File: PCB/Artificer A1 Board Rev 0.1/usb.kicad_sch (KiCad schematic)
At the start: 8 parts, among them U11 CH217K, U3 CH334F_C5187527, X1 SMD-3225_4P12M12PF10PPM

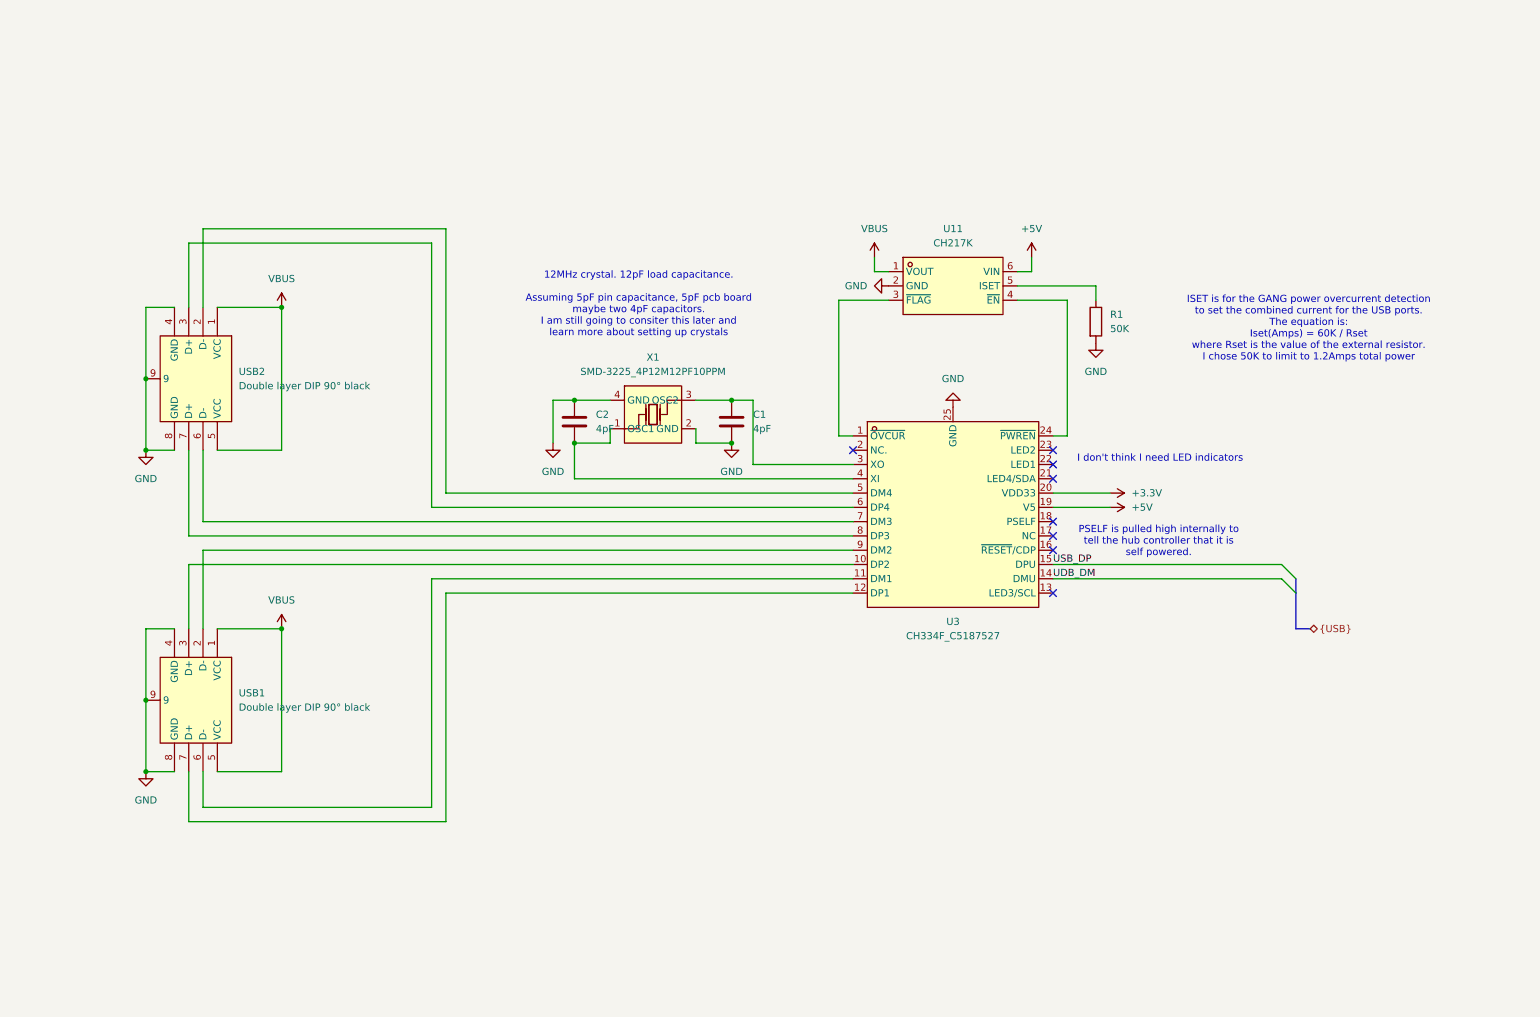
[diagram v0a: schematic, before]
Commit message: schematic update
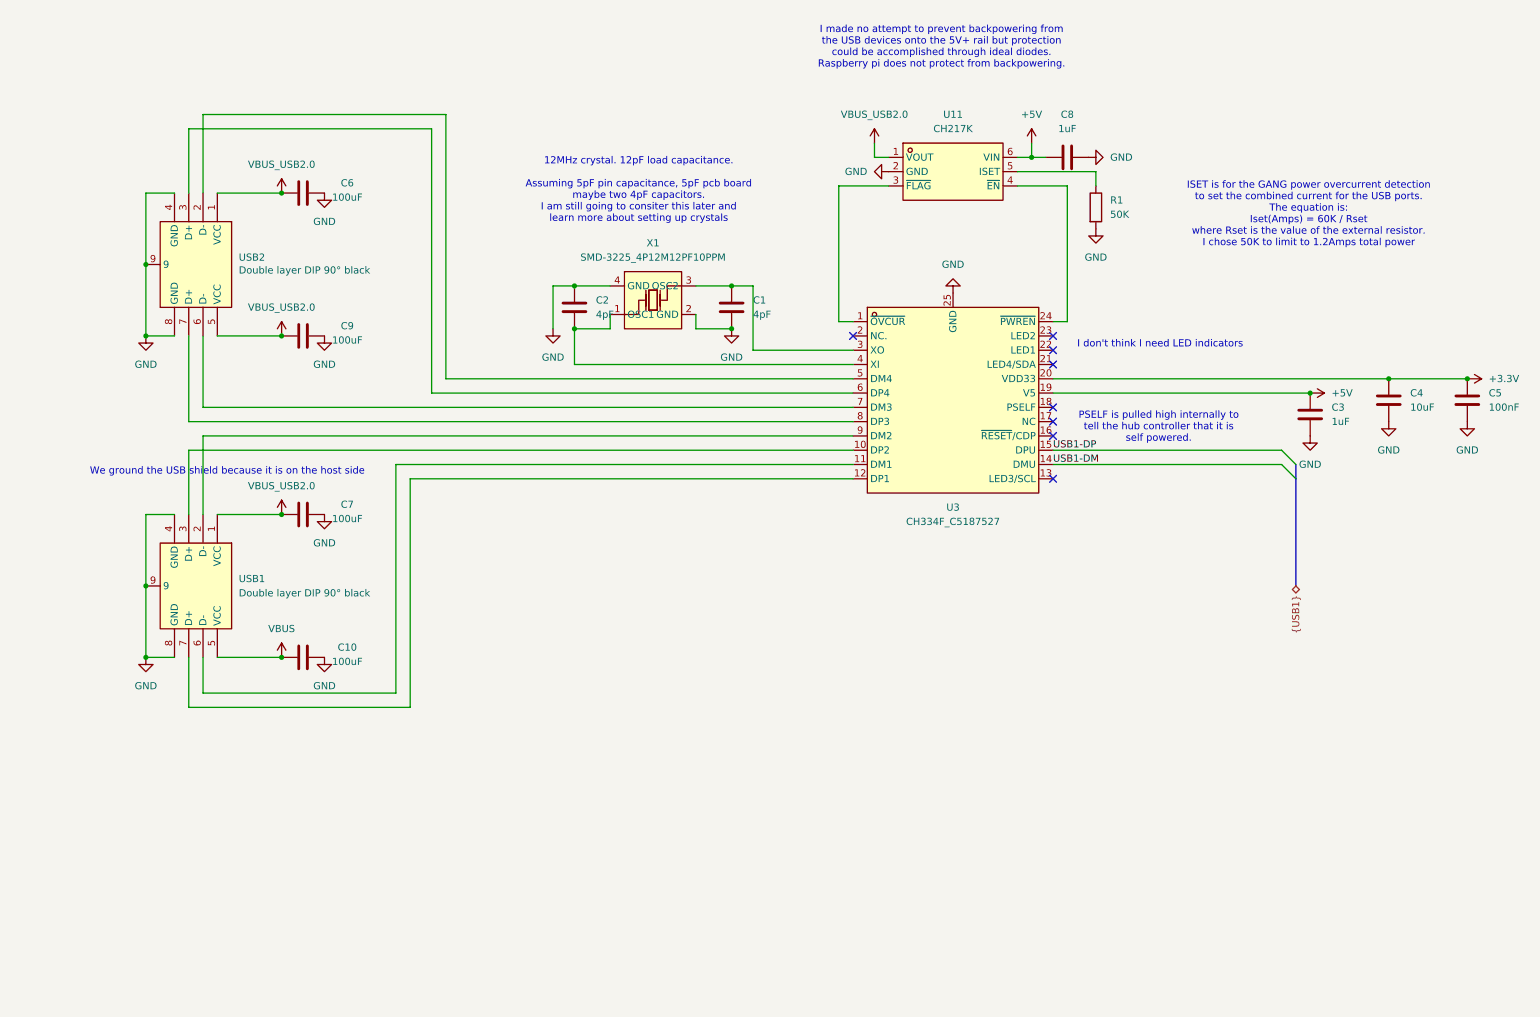
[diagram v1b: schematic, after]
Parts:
- added C10, C6, C7, C9: 100uF, symbol Device:C
- added C3, C8: 1uF, symbol Device:C
- added C4: 10uF, symbol Device:C
- added C5: 100nF, symbol Device:C
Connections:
- net +3.3V: now also C4.1, C5.1
- net +5V: now also C3.1, C8.1
- net GND: now also C10.2, C3.2, C4.2, C5.2, C6.2, C7.2, C8.2, C9.2
- net VBUS: now also C10.1; no longer U11.1 (VOUT), USB1.1 (VCC), USB2.1 (VCC), USB2.5 (VCC)
- net UDB_DM renamed USB1-DM
- net USB_DP renamed USB1-DP
- new net VBUS_USB2.0: C6.1, C7.1, C9.1, U11.1 (VOUT), USB1.1 (VCC), USB2.1 (VCC), USB2.5 (VCC)
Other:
- note added: "I made no attempt to prevent backpowering from the USB devices onto the 5V+ rail but protection could be accomplished through ideal diodes. Raspberry pi does not protect from backpowering."
- note added: "We ground the USB shield because it is on the host side"
- moved on the sheet: C1, C2, R1, U11, U3, USB1, USB2, X1

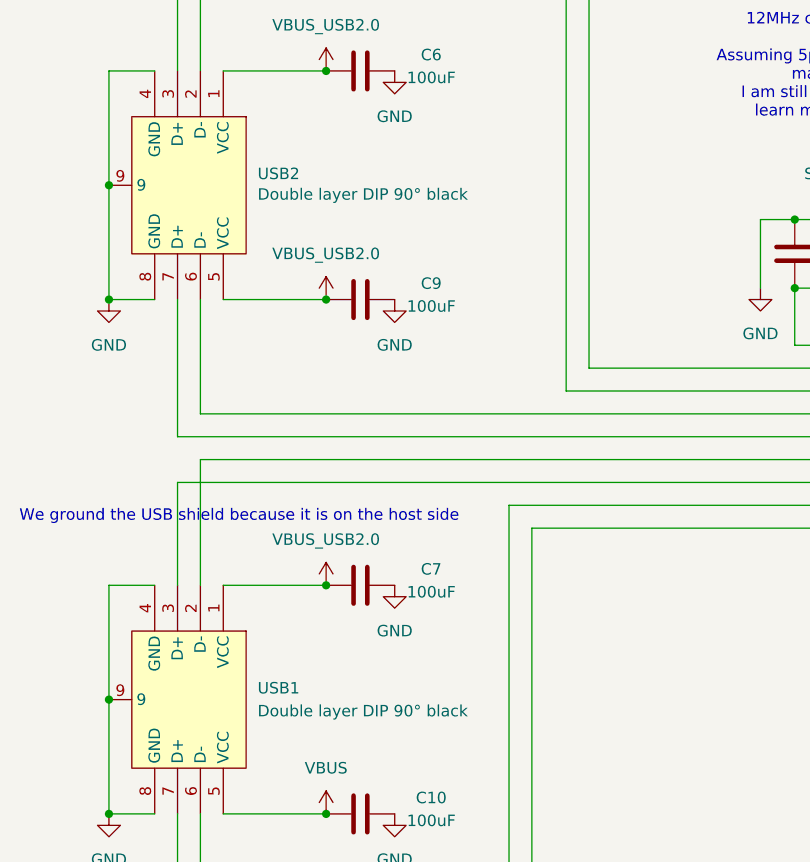
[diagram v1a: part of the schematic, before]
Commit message: localized libraries
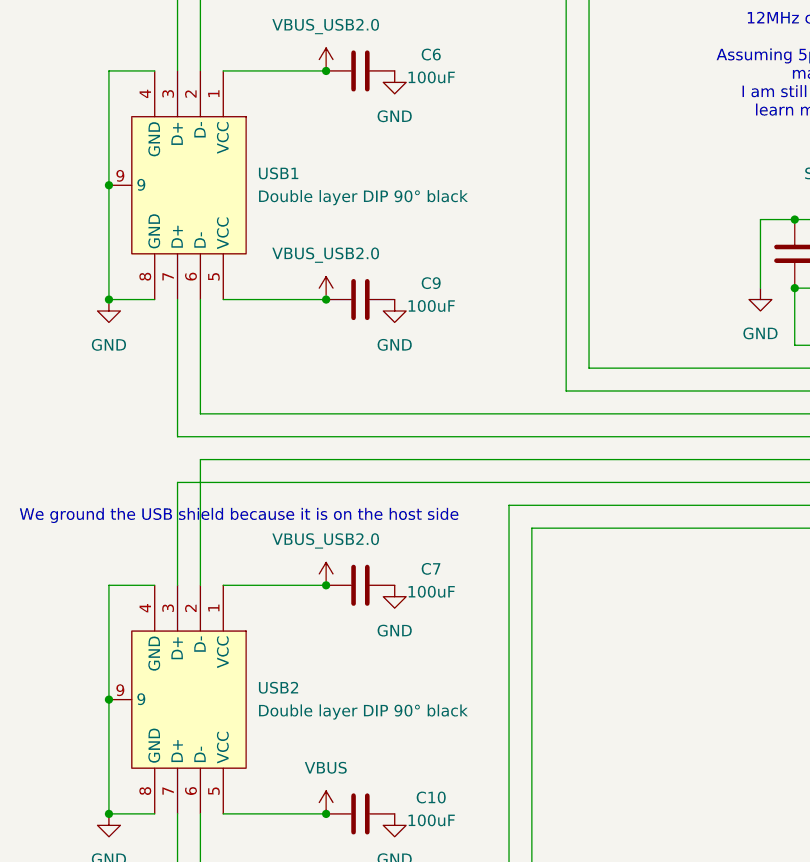
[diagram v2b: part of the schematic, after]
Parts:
- removed U11: CH217K, easyeda2kicad:SOT-23-6_L2.9-W1.6-P0.95-LS2.8-BL, symbol easyeda2kicad:CH217K
- removed U3: CH334F_C5187527, easyeda2kicad:QFN-24_L4.0-W4.0-P0.50-BL-EP2.8, symbol easyeda2kicad:CH334F_C5187527
- removed USB1, USB2: Double layer DIP 90° black, easyeda2kicad:USB-A-TH_USB-M-51, symbol easyeda2kicad:DoublelayerDIP90°black
- removed X1: SMD-3225_4P12M12PF10PPM, easyeda2kicad:CRYSTAL-SMD_4P-L3.2-W2.5-BL, symbol easyeda2kicad:SMD-3225_4P12M12PF10PPM
- added U11: CH217K, easyeda:SOT-23-6_L2.9-W1.6-P0.95-LS2.8-BL, symbol easyeda:CH217K
- added U3: CH334F_C5187527, easyeda:QFN-24_L4.0-W4.0-P0.50-BL-EP2.8, symbol easyeda:CH334F_C5187527
- added USB1, USB2: Double layer DIP 90° black, easyeda:USB-A-TH_USB-M-51, symbol easyeda:DoublelayerDIP90°black
- added X1: SMD-3225_4P12M12PF10PPM, easyeda:CRYSTAL-SMD_4P-L3.2-W2.5-BL, symbol easyeda:SMD-3225_4P12M12PF10PPM
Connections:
- net +3.3V: now also U3.20 (VDD33)
- net +5V: now also U11.6 (VIN), U3.19 (V5)
- net GND: now also U11.2 (GND), U3.25 (GND), USB1.4 (GND), USB1.8 (GND), USB1.9, USB2.4 (GND), USB2.8 (GND), USB2.9, X1.2 (GND), X1.4 (GND)
- net USB1-DM: now also U3.14 (DMU)
- net USB1-DP: now also U3.15 (DPU)
- net VBUS: now also USB2.5 (VCC)
- net VBUS_USB2.0: now also U11.1 (VOUT), USB1.1 (VCC), USB1.5 (VCC), USB2.1 (VCC)
- net at R1.1: now also U11.5 (ISET)
- net at C1.1: now also U3.3 (XO), X1.3 (OSC2)
- net at C2.2: now also U3.4 (XI), X1.1 (OSC1)
- new net: U11.3 (~{FLAG}), U3.1 (~{OVCUR})
- new net: U3.10 (DP2), USB2.3 (D+)
- new net: U3.11 (DM1), USB2.6 (D-)
- new net: U3.12 (DP1), USB2.7 (D+)
- new net: U11.4 (~{EN}), U3.24 (~{PWREN})
- new net: U3.5 (DM4), USB1.2 (D-)
- new net: U3.6 (DP4), USB1.3 (D+)
- new net: U3.7 (DM3), USB1.6 (D-)
- new net: U3.8 (DP3), USB1.7 (D+)
- new net: U3.9 (DM2), USB2.2 (D-)

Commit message: added a few accessories
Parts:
- added C13: 100uF, symbol Device:C
- added C14: 1uF, symbol Device:C
- added R3: 120k, symbol Device:R
- added U5: CH217K, easyeda:SOT-23-6_L2.9-W1.6-P0.95-LS2.8-BL, symbol easyeda:CH217K
- added U6: GT-USB-7010ASV, easyeda:USB-C-SMD_G-SWITCH_GT-USB-7010ASV, symbol easyeda:GT-USB-7010ASV
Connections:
- net +5V: now also C14.2, U5.6 (VIN)
- net GND: now also C13.1, C14.1, R3.2, U5.2 (GND), U5.4 (~{EN}), U6.1 (SHELL), U6.2 (SHELL), U6.3 (SHELL), U6.4 (SHELL), U6.A1B12 (GND), U6.B1A12 (GND)
- new net: C13.2, U5.1 (VOUT), U6.A4B9 (VBUS), U6.B4A9 (VBUS)
- new net: R3.1, U5.5 (ISET)
- new net CC1: U6.A5 (CC1)
- new net CC2: U6.B5 (CC2)
- new net DM: U6.A7 (DN1), U6.B7 (DN2)
- new net DP: U6.A6 (DP1), U6.B6 (DP2)
- new net UART0_RX: U6.B8 (SBU2)
- new net UART0_TX: U6.A8 (SBU1)
- no-connect marks 8 -> 9
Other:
- moved on the sheet: C1, C10, C2, C3, C4, C5, C6, C7, C8, C9, R1, U11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

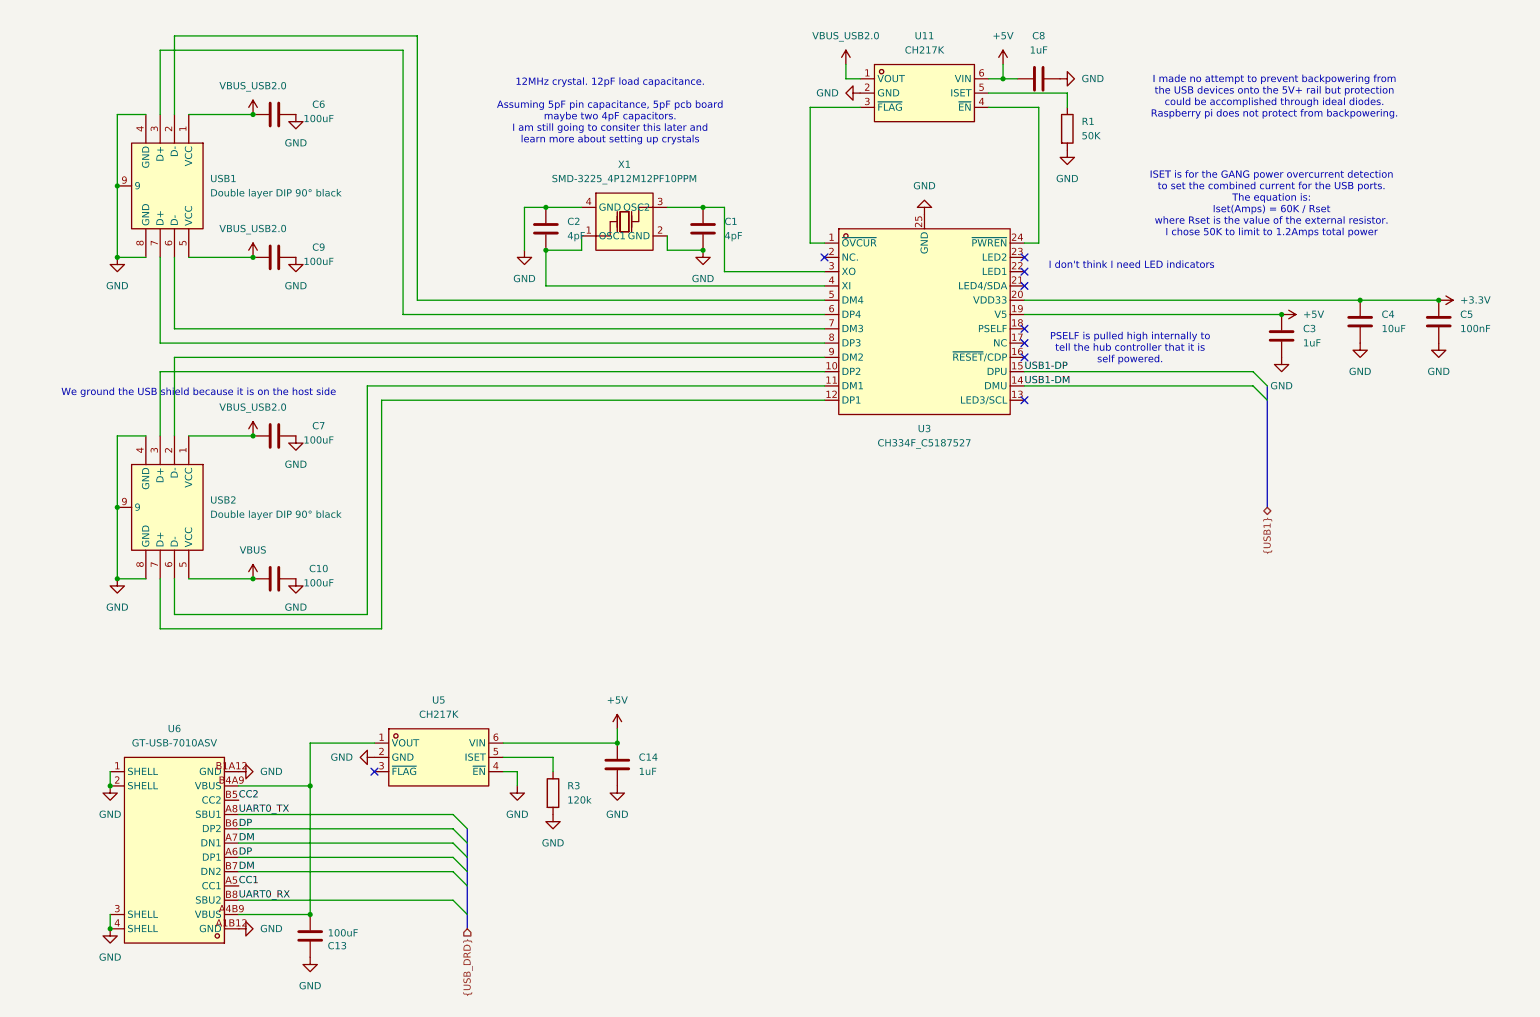
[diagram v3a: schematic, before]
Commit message: added HDMI, DP, DSI, etc
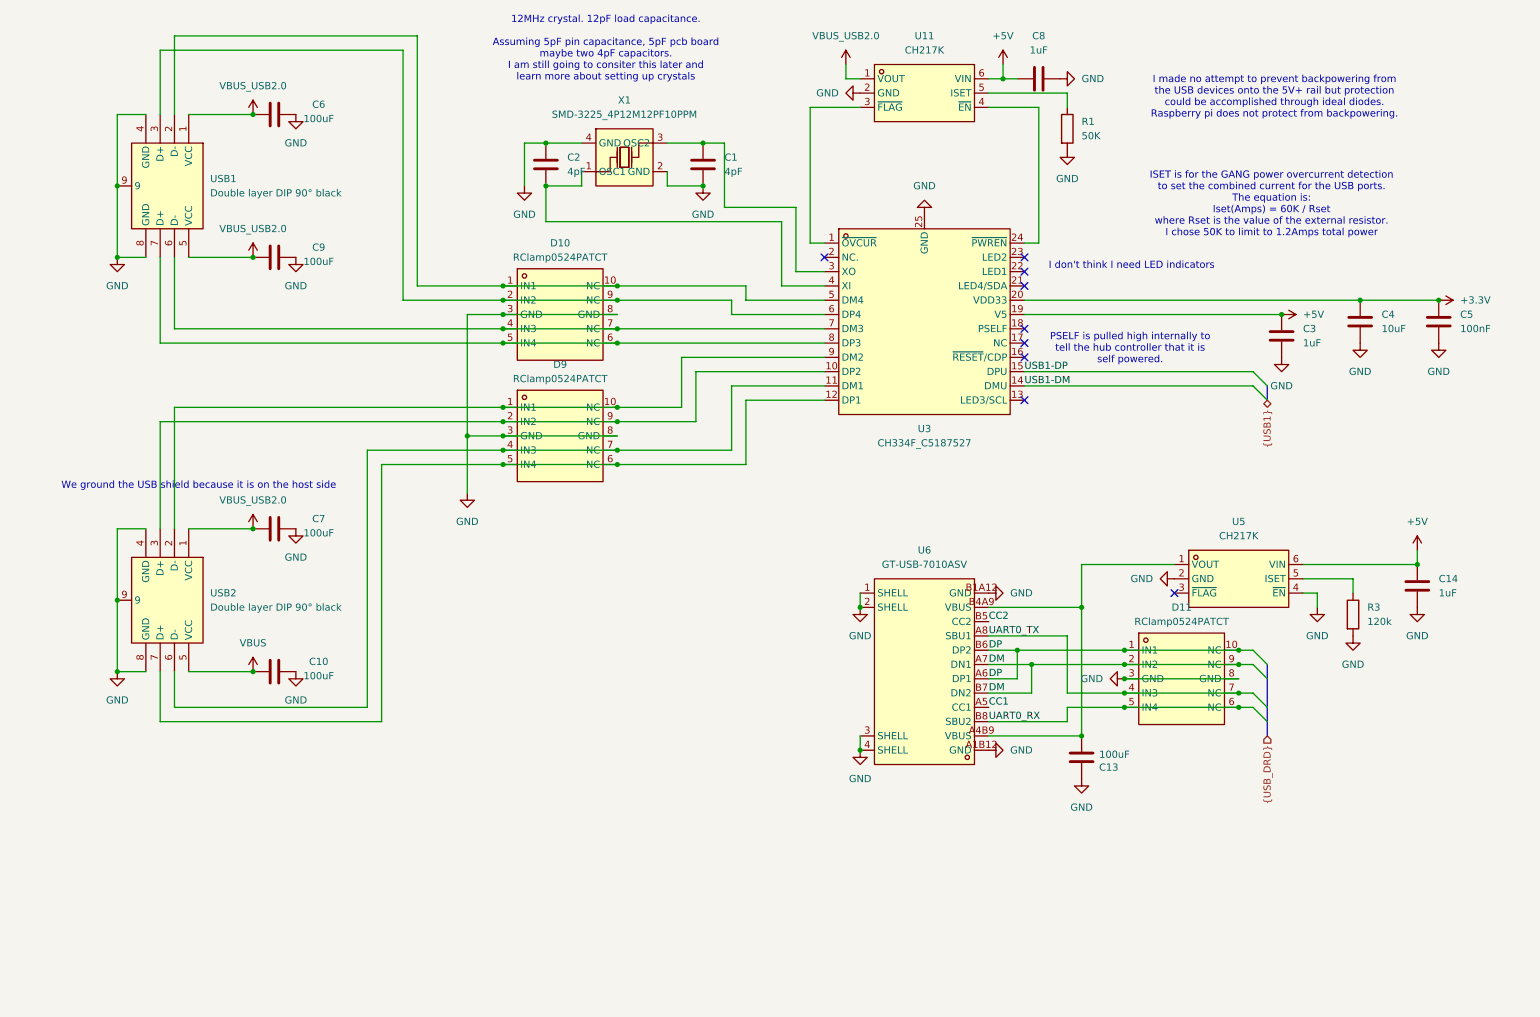
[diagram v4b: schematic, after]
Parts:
- added D10, D11, D9: RClamp0524PATCT, easyeda:SLP2510P8_L2.5-W1.0-P0.50-BL, symbol easyeda:RClamp0524PATCT
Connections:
- net DM: now also D11.2 (IN2), D11.9 (NC)
- net DP: now also D11.1 (IN1), D11.10 (NC)
- net GND: now also D10.3 (GND), D10.8 (GND), D11.3 (GND), D11.8 (GND), D9.3 (GND), D9.8 (GND)
- net UART0_RX: now also D11.5 (IN4), D11.6 (NC)
- net UART0_TX: now also D11.4 (IN3), D11.7 (NC)
- net at U3.10 (DP2), USB2.3 (D+): now also D9.2 (IN2), D9.9 (NC)
- net at U3.11 (DM1), USB2.6 (D-): now also D9.4 (IN3), D9.7 (NC)
- net at U3.12 (DP1), USB2.7 (D+): now also D9.5 (IN4), D9.6 (NC)
- net at U3.5 (DM4), USB1.2 (D-): now also D10.1 (IN1), D10.10 (NC)
- net at U3.6 (DP4), USB1.3 (D+): now also D10.2 (IN2), D10.9 (NC)
- net at U3.7 (DM3), USB1.6 (D-): now also D10.4 (IN3), D10.7 (NC)
- net at U3.8 (DP3), USB1.7 (D+): now also D10.5 (IN4), D10.6 (NC)
- net at U3.9 (DM2), USB2.2 (D-): now also D9.1 (IN1), D9.10 (NC)
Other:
- moved on the sheet: C1, C10, C13, C14, C2, C7, R3, U5, U6, USB2, X1
